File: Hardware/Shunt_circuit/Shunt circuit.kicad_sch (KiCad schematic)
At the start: 40 parts, among them J1 Vbus, J2 Shunt Voltage Measuring Points, J3 POWER CONNECTOR (from the stm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, J4 IC2 SIGNAL CONNECTOR, J5 ALERT CONNECTOR, U1 NXE1S0303MC, U2 INA238, U3 ISO1540, U4 ISO7710FQDRQ1

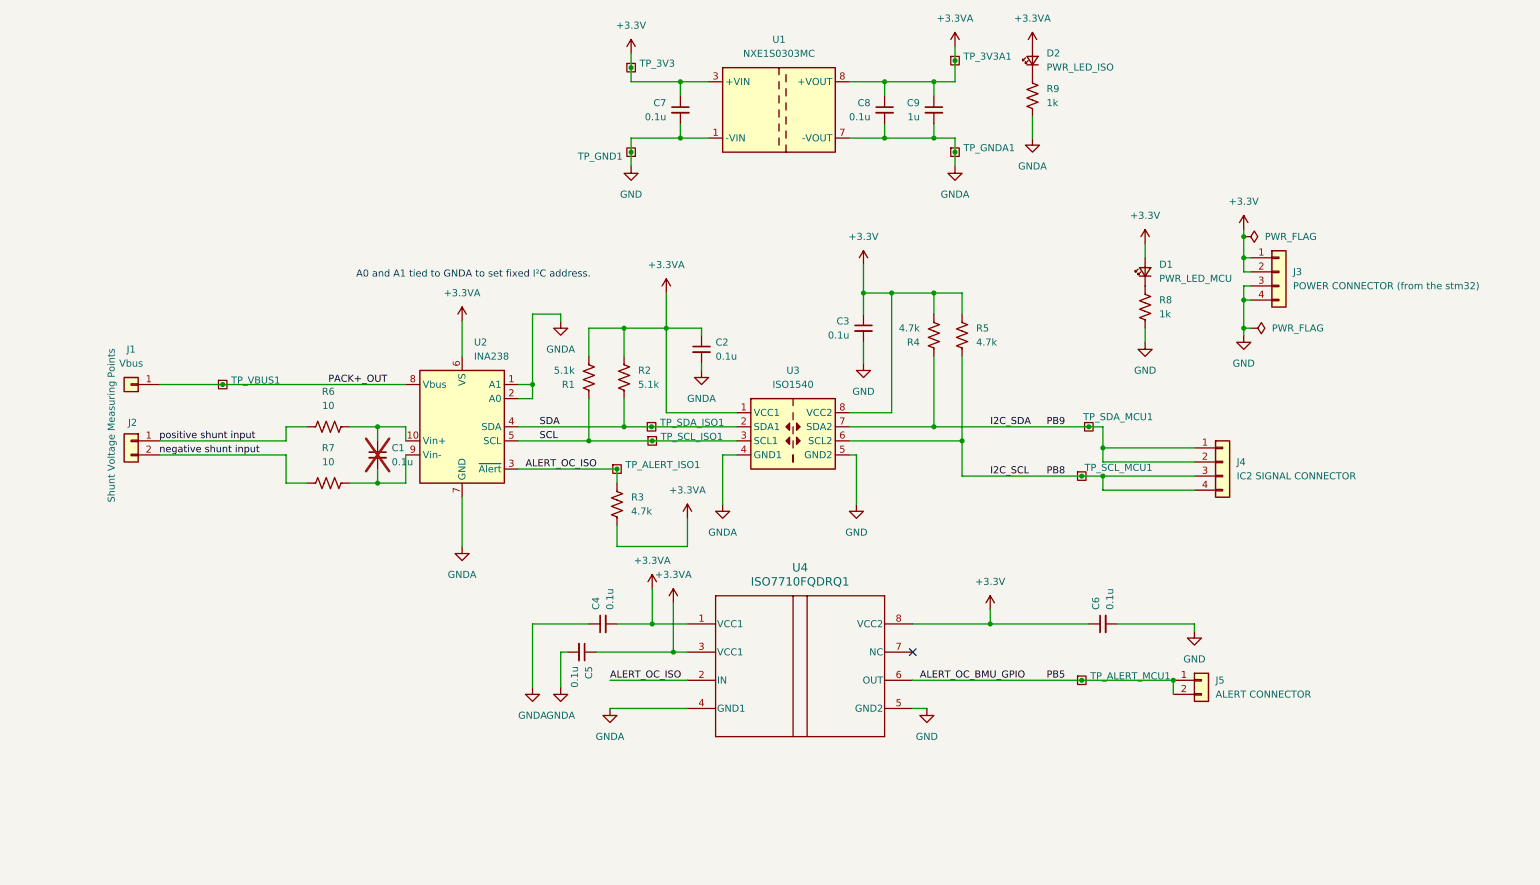
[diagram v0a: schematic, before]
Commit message: Replace shunt circuit libraries and update KiCad files
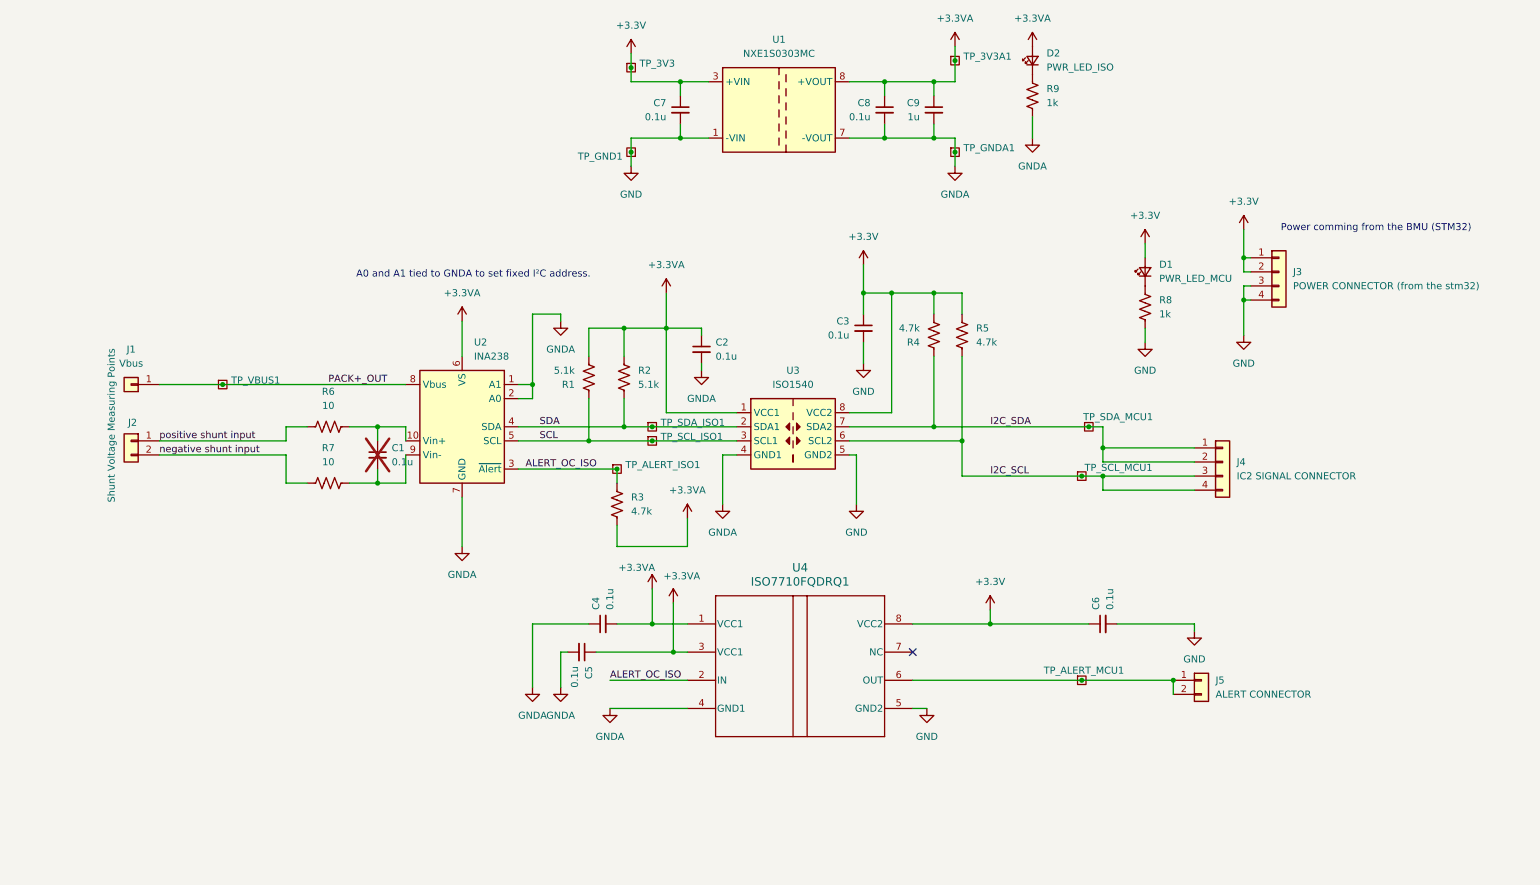
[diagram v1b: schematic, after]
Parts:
- U4: footprint footprints:D0008B_HV -> footprints1:D0008B_HV
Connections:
- net ALERT_OC_BMU_GPIO: no longer names the net of J5.1 (Pin_1), J5.2 (Pin_2), TP_ALERT_MCU1.1, U4.6 (OUT)
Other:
- note added: "Power comming from the BMU (STM32)"

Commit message: Fixed shunt board, fixed .gitignore.
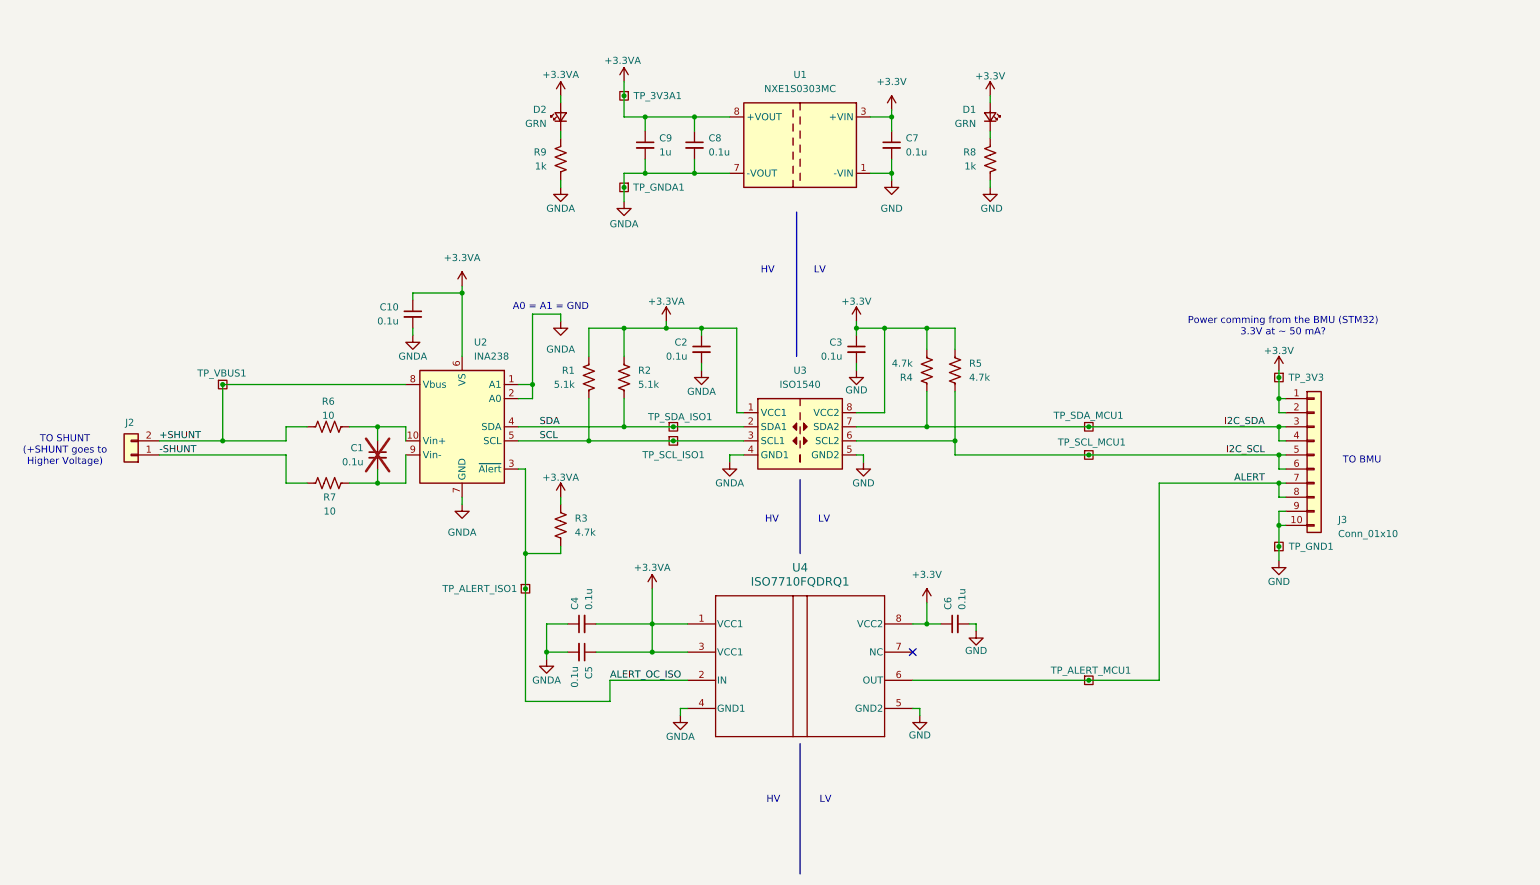
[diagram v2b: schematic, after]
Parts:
- removed J1: Vbus, Connector_PinHeader_2.54mm:PinHeader_1x01_P2.54mm_Vertical, symbol Connector_Generic:Conn_01x01
- removed J3: POWER CONNECTOR (from the stm32), Connector_PinHeader_2.54mm:PinHeader_1x04_P2.54mm_Vertical, symbol Connector_Generic:Conn_01x04
- removed J4: IC2 SIGNAL CONNECTOR, Connector_PinHeader_2.54mm:PinHeader_1x04_P2.54mm_Vertical, symbol Connector_Generic:Conn_01x04
- removed J5: ALERT CONNECTOR, Connector_PinHeader_2.54mm:PinHeader_1x02_P2.54mm_Vertical, symbol Connector_Generic:Conn_01x02
- added C10: 0.1u, Capacitor_SMD:C_0805_2012Metric, symbol Device:C_Small
- added J3: Conn_01x10, Connector_PinHeader_2.54mm:PinHeader_1x10_P2.54mm_Vertical, symbol Connector_Generic:Conn_01x10
- D1: value PWR_LED_MCU -> GRN
- D2: value PWR_LED_ISO -> GRN
- TP_3V3, TP_3V3A1, TP_ALERT_ISO1, TP_ALERT_MCU1, TP_GND1, TP_GNDA1, TP_SCL_ISO1, TP_SCL_MCU1, TP_SDA_ISO1, TP_SDA_MCU1, TP_VBUS1: now left out of the parts list
- U4: footprint footprints1:D0008B_HV -> footprints:D0008B_HV; symbol 2026-04-14_20-51-37:ISO7710FQDRQ1 -> ISO7710FQDRQ1:ISO7710FQDRQ1
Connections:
- net +3.3V: now also J3.1 (Pin_1), J3.2 (Pin_2)
- net +3.3VA: now also R1.1, C10.1; no longer R1.2
- net GND: now also J3.10 (Pin_10), J3.9 (Pin_9)
- net GNDA: now also C10.2
- net I2C_SCL: now also J3.5 (Pin_5), J3.6 (Pin_6)
- net I2C_SDA: now also J3.3 (Pin_3), J3.4 (Pin_4)
- net SCL: now also R1.2; no longer R1.1
- net ALERT: now reaches TP_ALERT_MCU1.1, U4.6 (OUT)
- net ALERT: now also J3.7 (Pin_7), J3.8 (Pin_8)
- net PACK+_OUT renamed +SHUNT
- net +SHUNT: now also J2.2 (Pin_2), R6.1
- net negative shunt input renamed -SHUNT
- net -SHUNT: now also J2.1 (Pin_1); no longer J2.2 (Pin_2)
- removed net positive shunt input: J2.1 (Pin_1), R6.1
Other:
- note added: "A0 = A1 = GND"
- note added: "HV"
- note added: "LV"
- note added: "Power comming from the BMU (STM32) 3.3V at ~ 50 mA?"
- note added: "TO BMU"
- note added: "TO SHUNT (+SHUNT goes to Higher Voltage)"
- note removed: "A0 and A1 tied to GNDA to set fixed I²C address."
- note removed: "Power comming from the BMU (STM32)"
- title: Shunt Current Sense Circiut -> Current Sense Board
- moved on the sheet: C3, C4, C6, C7, C8, C9, D1, D2, J2, R1, R3, R4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

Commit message: doubled up pin for bmu
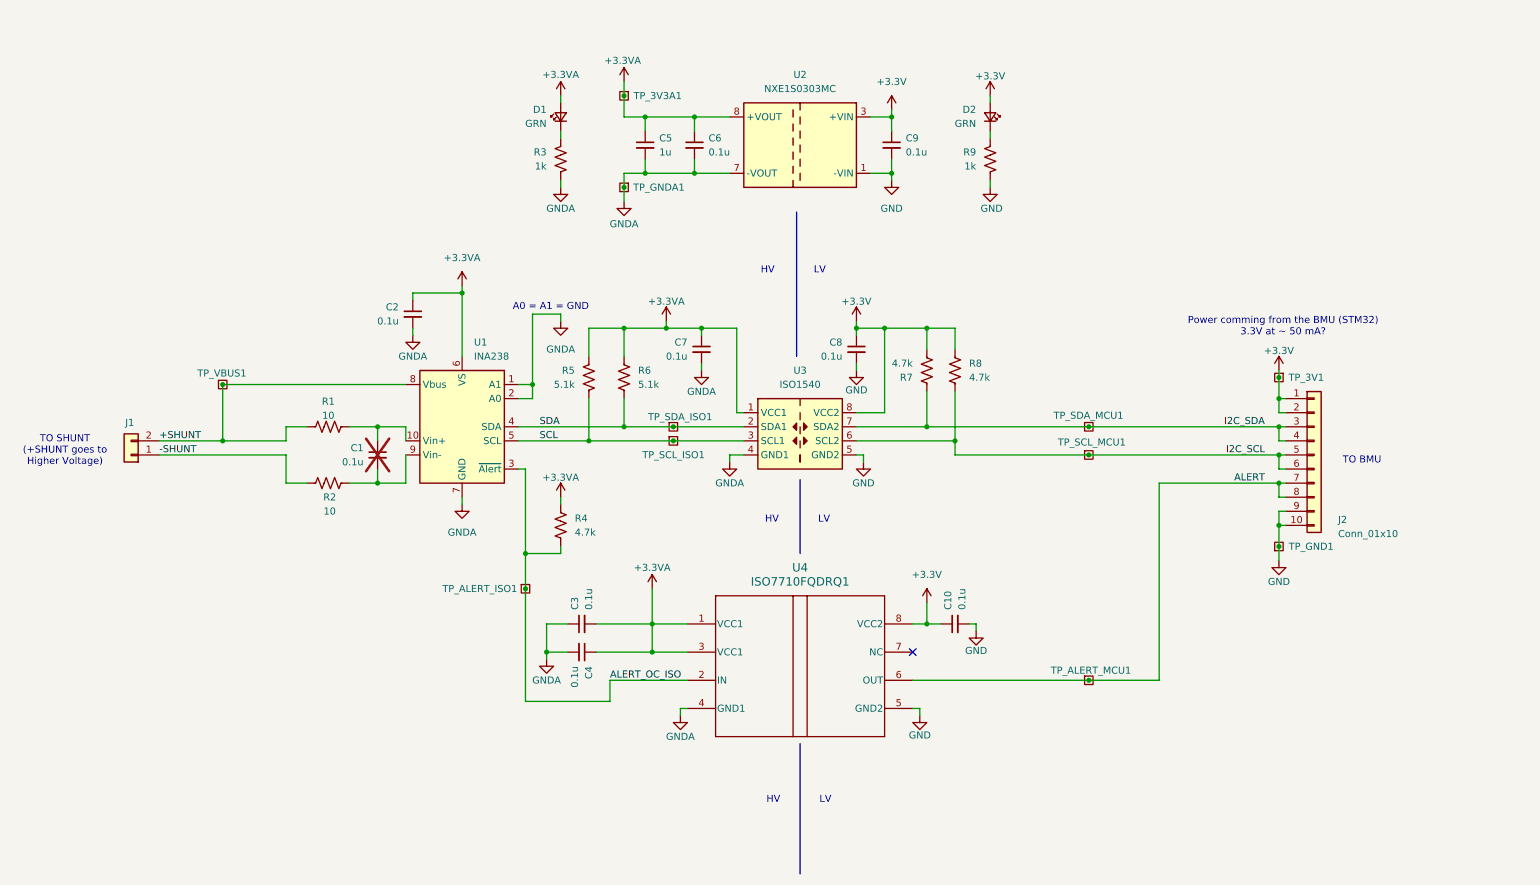
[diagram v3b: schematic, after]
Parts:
- renumbered C6 to C10, C10 to C2, C4 to C3, C5 to C4, C9 to C5, C8 to C6, C2 to C7, C3 to C8, C7 to C9, D2 to D1, D1 to D2, J2 to J1, J3 to J2, R6 to R1, R7 to R2, R9 to R3, R3 to R4, R1 to R5, R2 to R6, R4 to R7, R5 to R8, R8 to R9, TP_3V3 to TP_3V1, U2 to U1, U1 to U2

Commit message: Update shunt circuit files and add BOM
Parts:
- C10, C2, C3, C4, C6, C7, C8, C9: DIS (none) -> DigiKey; DPN (none) -> 311-1140-1-ND; MFR (none) -> YAGEO; MPN (none) -> CC0805KRX7R9BB104
- C5: DIS (none) -> DigiKey; DPN (none) -> 311-1365-1-ND; MFR (none) -> YAGEO; MPN (none) -> CC0805KKX7R7BB105
- D1: DIS (none) -> DigiKey; DPN (none) -> 160-1415-2-ND; MFR (none) -> Lite-On; MPN (none) -> LTST-C170KRKT
- D2: DIS (none) -> DigiKey; DPN (none) -> 160-1179-1-ND; MFR (none) -> Lite-On; MPN (none) -> LTST-C170GKT
- J1: DIS (none) -> DigiKey; DPN (none) -> 277-1263-ND; MFR (none) -> Phoenix Contact; MPN (none) -> 1715721
- J2: DIS (none) -> DigiKey; DPN (none) -> S1011EC-10-ND; MFR (none) -> Sullins Connector Solutions; MPN (none) -> PRPC010SAAN-RC
- R1, R2: DIS (none) -> DigiKey; DPN (none) -> 311-10.0CRCT-ND; MFR (none) -> YAGEO; MPN (none) -> RC0805FR-0710RL
- R3, R9: DIS (none) -> DigiKey; DPN (none) -> 311-1.00KCRCT-ND; MFR (none) -> YAGEO; MPN (none) -> RC0805FR-071KL
- R4, R7, R8: DIS (none) -> DigiKey; DPN (none) -> 311-4.70KCRCT-ND; MFR (none) -> YAGEO; MPN (none) -> RC0805FR-074K7L
- R5, R6: DIS (none) -> DigiKey; DPN (none) -> 311-5.10KCRCT-ND; MFR (none) -> YAGEO; MPN (none) -> RC0805FR-075K1L
- U1: DIS (none) -> N/A; DPN (none) -> 296-INA238AQDGSRQ1CT-ND; MFR (none) -> Texas Instruments; MPN (none) -> INA238AQDGSRQ1
- U2: DIS (none) -> DigiKey; DPN (none) -> 811-3479-1-ND; MFR (none) -> Murata Power Solutions; MPN (none) -> NXF1S0303MC-R7
- U3: DIS (none) -> DigiKey; DPN (none) -> 296-45354-1-ND; MFR (none) -> Texas Instruments; MPN (none) -> ISO1540QDRQ1
- U4: DIS (none) -> DigiKey; DPN (none) -> 296-51196-1-ND; MFR (none) -> Texas Instruments; MPN (none) -> ISO7710FQDRQ1

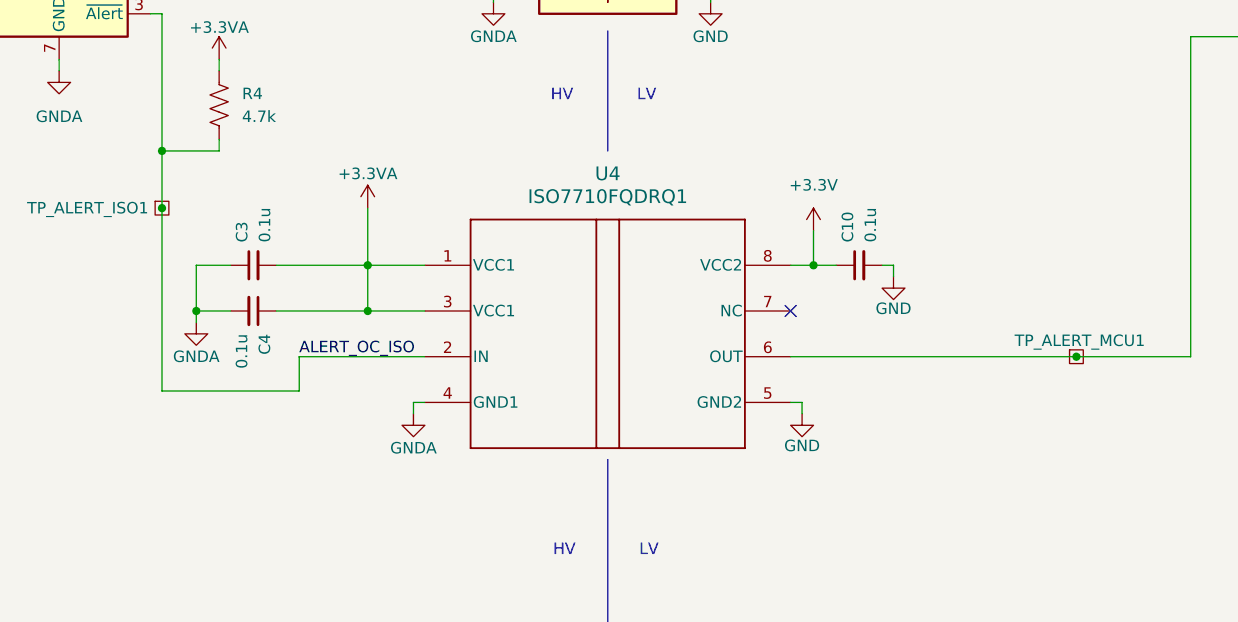
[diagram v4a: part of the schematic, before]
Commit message: Made a nicer symbol, cleaned up ERC, cleaned up DRC, fabricated
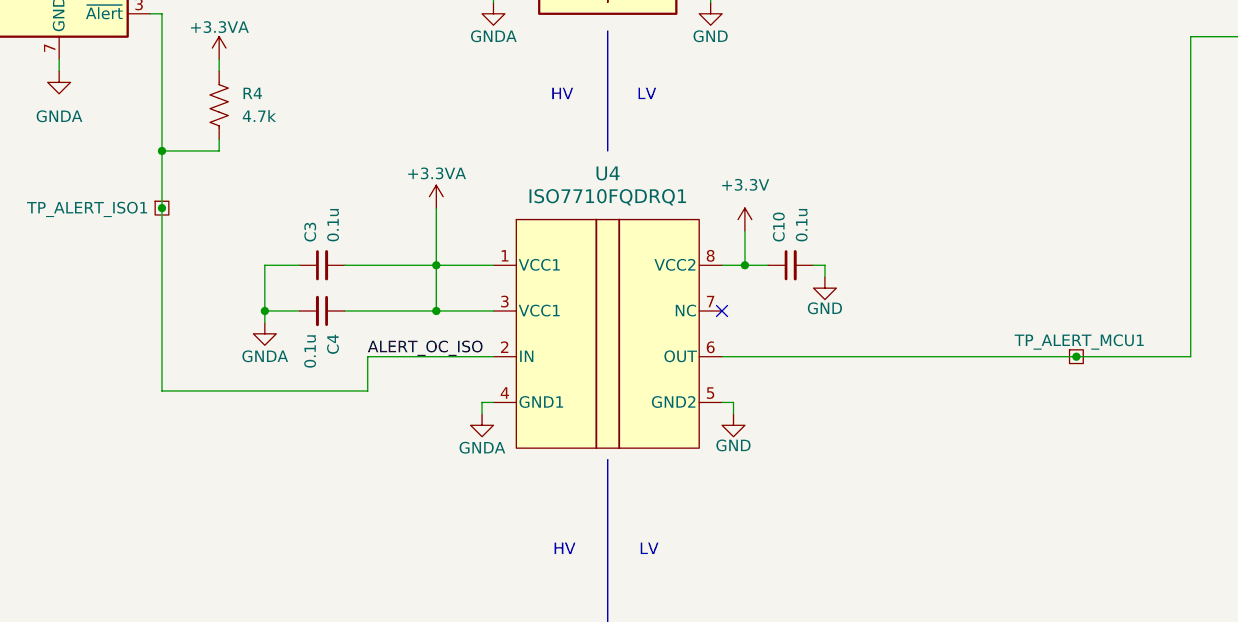
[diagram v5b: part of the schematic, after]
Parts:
- U4: footprint footprints:D0008B_HV -> footprints:D0008B_N
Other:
- moved on the sheet: C10, C3, C4
